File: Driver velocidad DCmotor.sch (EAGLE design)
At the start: 11 parts

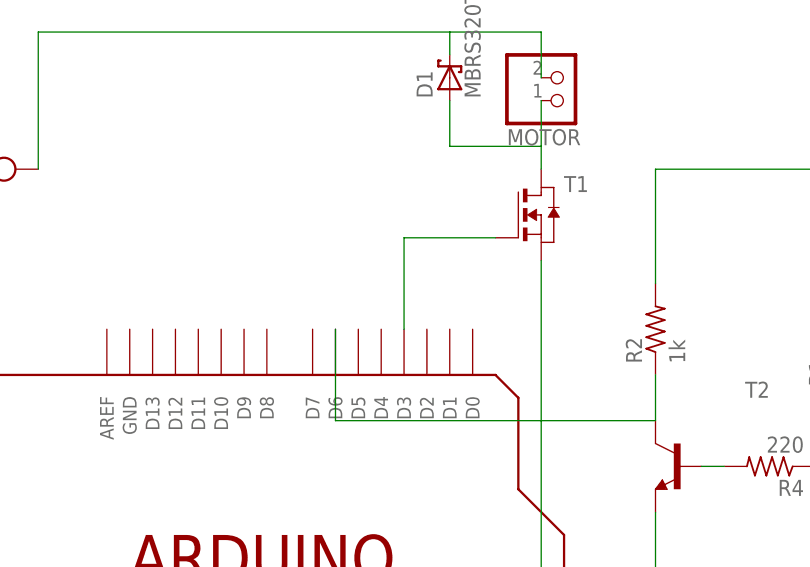
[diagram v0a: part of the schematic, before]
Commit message: se agrega la resistencia de 330 Ohms a la compuerta del MOSFET
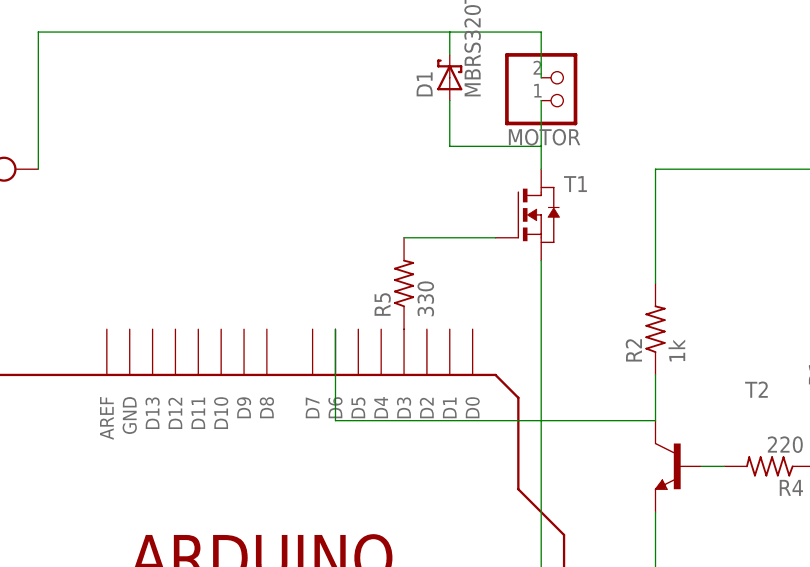
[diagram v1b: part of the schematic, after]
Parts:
- added R5: 330, adafruit:R-US_M1206
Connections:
- new net N$15: R5.1, U$1.D3
- net N$8: now also R5.2; no longer U$1.D3
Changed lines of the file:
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@@
 <part name="R3" library="adafruit" deviceset="R-US_" device="M1206" value="220"/>
 <part name="R4" library="adafruit" deviceset="R-US_" device="M1206" value="220"/>
+<part name="R5" library="adafruit" deviceset="R-US_" device="M1206" value="330"/>
 </parts>
 <sheets>
@@
 <instance part="R3" gate="G$1" x="88.9" y="30.48" rot="R90"/>
 <instance part="R4" gate="G$1" x="76.2" y="40.64" rot="R180"/>
+<instance part="R5" gate="G$1" x="35.56" y="60.96" rot="R90"/>
 </instances>
 <busses>
@@
 <pinref part="T1" gate="A" pin="G"/>
 <wire x1="45.72" y1="66.04" x2="35.56" y2="66.04" width="0.1524" layer="91"/>
-<pinref part="U$1" gate="G$1" pin="D3"/>
-<wire x1="35.56" y1="66.04" x2="35.56" y2="55.88" width="0.1524" layer="91"/>
+<pinref part="R5" gate="G$1" pin="2"/>
 </segment>
 </net>
@@
 </segment>
 </net>
+<net name="N$15" class="0">
+<segment>
+<pinref part="U$1" gate="G$1" pin="D3"/>
+<pinref part="R5" gate="G$1" pin="1"/>
+</segment>
+</net>
